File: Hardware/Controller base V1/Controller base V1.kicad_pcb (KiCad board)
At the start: 2 copper layers, 30 x 50 mm, 32 parts, among them J1 USB_C_Receptacle_USB2.0_16P, J3 Conn_02x10_Counter_Clockwise, J4 Conn_02x10_Counter_Clockwise, SW1 SW_Push, U1 AZ1117CH-3.3TRG1, U2 ESP32-S3-WROOM-1U-N4

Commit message: track update
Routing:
- net GND: track 72.2 -> 88.3 mm, vias 7 -> 11
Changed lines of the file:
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@@
+	)
+	(segment
+		(start 146.75 83.475)
+		(end 146.75 80.175)
+		(width 0.3)
+		(layer "F.Cu")
+		(net 1)
 	)
 	(segment
@@
 	)
 	(segment
+		(start 156.15 89.875)
+		(end 151.85 89.875)
+		(width 0.2)
+		(layer "F.Cu")
+		(net 1)
+	)
+	(segment
+		(start 151.85 89.875)
+		(end 146.75 84.775)
+		(width 0.2)
+		(layer "F.Cu")
+		(net 1)
+	)
+	(segment
 		(start 139.547624 75.985)
 		(end 138.93 75.985)
@@
 	(segment
 		(start 145.075 111)
-		(end 145.075 114.175)
+		(end 145.075 112.175)
 		(width 0.3)
 		(layer "F.Cu")
@@
 	)
 	(segment
+		(start 146.75 84.775)
+		(end 146.75 83.475)
+		(width 0.2)
+		(layer "F.Cu")
+		(net 1)
+	)
+	(segment
+		(start 145.075 112.175)
+		(end 145.075 114.175)
+		(width 0.3)
+		(layer "F.Cu")
+		(net 1)
+	)
+	(segment
 		(start 133.825 79.825)
 		(end 133.85 79.85)
@@
 	)
 	(via
+		(at 146.75 80.175)
+		(size 0.6)
+		(drill 0.3)
+		(layers "F.Cu" "B.Cu")
+		(net 1)
+	)
+	(via
+		(at 146.75 83.475)
+		(size 0.6)
+		(drill 0.3)
+		(layers "F.Cu" "B.Cu")
+		(free yes)
+		(net 1)
+	)
+	(via
 		(at 133.15 84.75)
 		(size 0.6)
@@
 	)
 	(via
+		(at 145.075 112.175)
+		(size 0.6)
+		(drill 0.3)
+		(layers "F.Cu" "B.Cu")
+		(net 1)
+	)
+	(via
 		(at 131.05 79.825)
 		(size 0.6)
 		(drill 0.3)
+		(layers "F.Cu" "B.Cu")
+		(net 1)
+	)
+	(via
+		(at 156.15 89.875)
+		(size 0.6)
+		(drill 0.3)

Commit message: update tracks
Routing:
- net GND: track 88.3 -> 85.0 mm, vias 11 -> 10
- net /CC2: track 6.91 -> 6.21 mm
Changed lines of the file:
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@@
-	)
-	(segment
-		(start 146.75 83.475)
-		(end 146.75 80.175)
-		(width 0.3)
-		(layer "F.Cu")
-		(net 1)
 	)
 	(segment
@@
 	)
 	(via
-		(at 146.75 80.175)
-		(size 0.6)
-		(drill 0.3)
-		(layers "F.Cu" "B.Cu")
-		(net 1)
-	)
-	(via
 		(at 146.75 83.475)
 		(size 0.6)
@@
 	)
 	(segment
-		(start 141.475 78.675)
-		(end 141.21 78.41)
+		(start 141.5125 78.325)
+		(end 141.21 78.0225)
 		(width 0.2)
 		(layer "F.Cu")
@@
 	)
 	(segment
-		(start 141.21 78.41)
+		(start 141.21 78.0225)
 		(end 141.21 76.92)
 		(width 0.2)
@@
 	)
 	(via
-		(at 141.475 78.675)
+		(at 141.5125 78.325)
 		(size 0.6)
 		(drill 0.3)
@@
 	)
 	(segment
-		(start 141.5125 78.6375)
-		(end 141.475 78.675)
-		(width 0.2)
-		(layer "B.Cu")
-		(net 12)
-	)
-	(segment
-		(start 141.5125 73.65)
-		(end 141.5125 78.6375)
-		(width 0.2)
-		(layer "B.Cu")
+		(start 141.5125 78.325)
+		(end 141.5125 73.65)
+		(width 0.2)
+		(layer "B.Cu")

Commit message: update
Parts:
- moved C7 1.82 mm to (149.1, 112.7)
- moved C5 1.78 mm to (149.1, 111.0)
- moved R6 1.52 mm to (148.6, 116.2)
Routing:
- net ESP_3.3V: track 13.7 -> 11.5 mm
- net GND: track 85.0 -> 86.3 mm, vias 10 -> 23

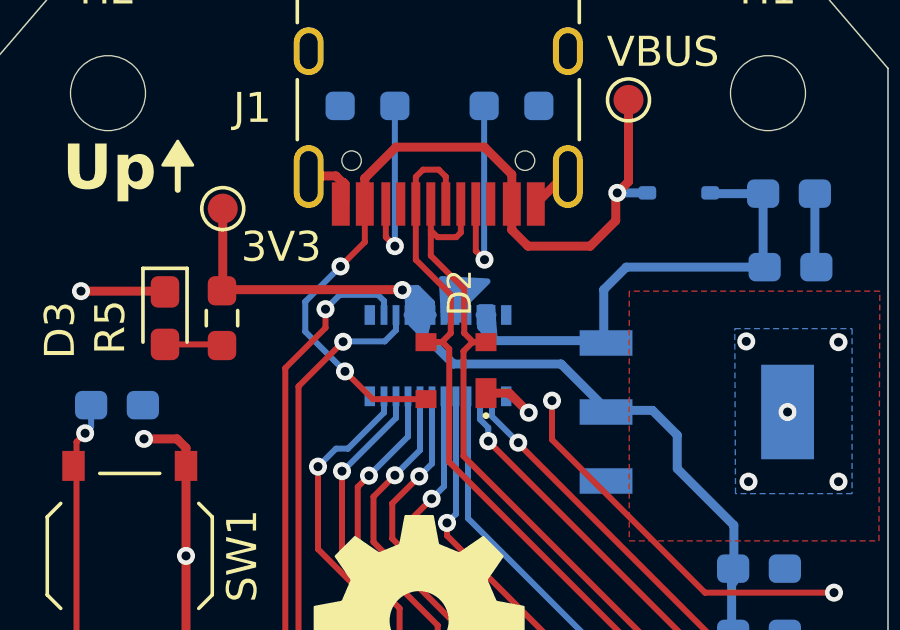
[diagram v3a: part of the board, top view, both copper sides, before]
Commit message: trace update
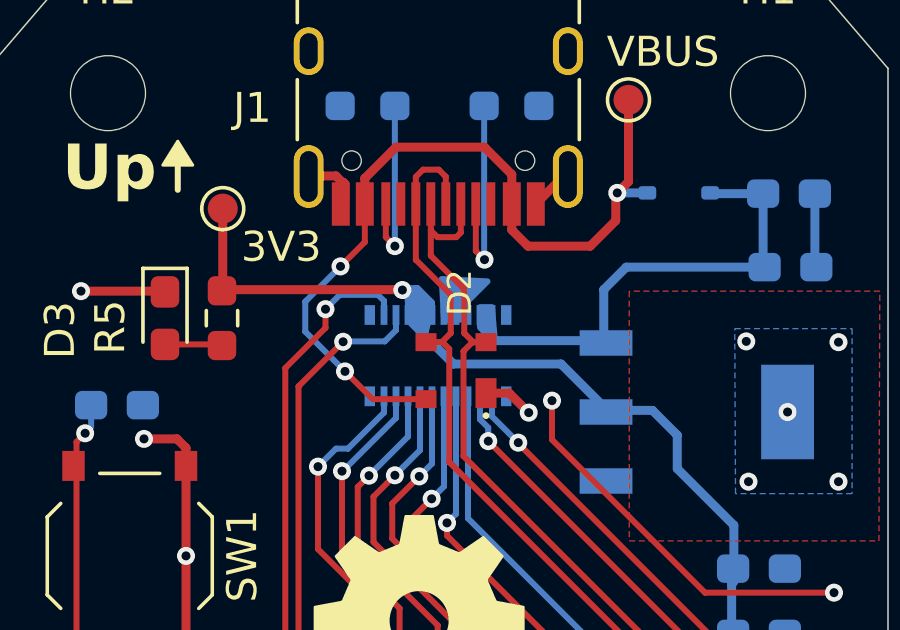
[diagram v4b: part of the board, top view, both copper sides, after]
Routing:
- net VCC_3V3: track 60.3 -> 59.4 mm
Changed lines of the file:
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@@
-	)
-	(segment
-		(start 142.75 80.62)
-		(end 142.595 80.62)
-		(width 0.3)
-		(layer "B.Cu")
-		(net 2)
 	)
 	(segment
@@
 		(start 150.9625 93.125)
 		(end 152.375 93.125)
-		(width 0.3)
-		(layer "B.Cu")
-		(net 2)
-	)
-	(segment
-		(start 141.95 80.62)
-		(end 142.75 80.62)
 		(width 0.3)
 		(layer "B.Cu")
@@
 	)
 	(segment
-		(start 144.575 80.62)
-		(end 144.75 80.62)
-		(width 0.3)
-		(layer "B.Cu")
-		(net 4)
-	)
-	(segment
 		(start 153.8375 79.025)
 		(end 149.225 79.025)
@@
 		(width 0.3)
 		(layer "B.Cu")
-		(net 4)
-	)
-	(segment
-		(start 144.35 80.62)
-		(end 144.575 80.62)
-		(width 0.3)
-		(layer "B.Cu")

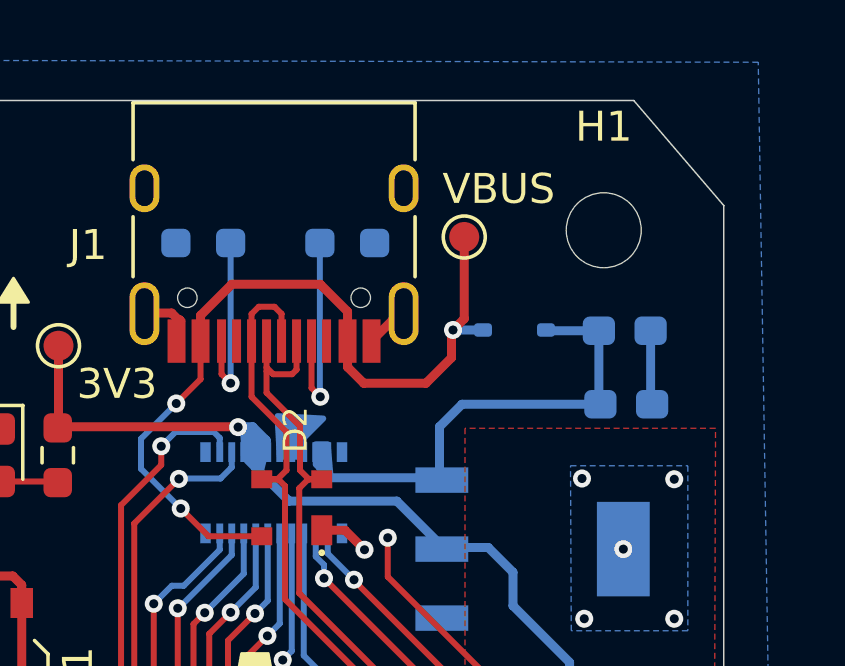
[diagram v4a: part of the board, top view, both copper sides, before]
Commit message: updated power trace for expansion
made where there is 5v to carrier board for future batter expansion
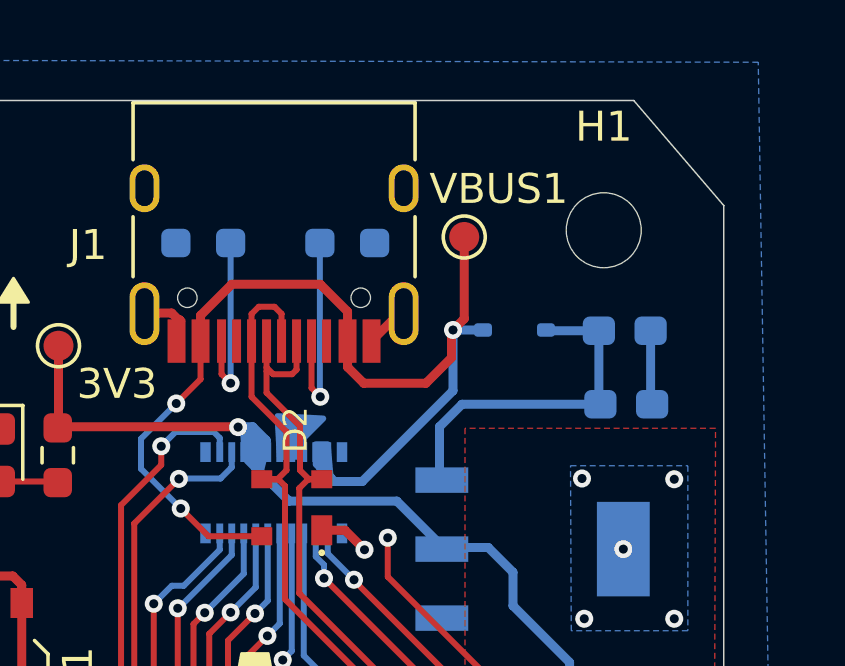
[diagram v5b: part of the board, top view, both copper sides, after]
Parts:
- renumbered VBUS to VBUS1
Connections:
- J3 pad 18: VCC_5V -> VBUS
- J3 pad 20: VCC_5V -> VBUS
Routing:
- net VBUS: track 27.7 -> 36.8 mm
- net VCC_5V: track 16.4 -> 11.7 mm
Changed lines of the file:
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@@
 		(descr "SMD pad as test Point, diameter 1.0mm")
 		(tags "test point SMD pad")
-		(property "Reference" "VBUS"
+		(property "Reference" "VBUS1"
 			(at 1.15 -1.6 0)
 			(layer "F.SilkS")
@@
 			(size 0.23 0.66)
 			(layers "B.Cu" "B.Mask" "B.Paste")
-			(net 4 "VCC_5V")
+			(net 5 "VBUS")
 			(pinfunction "18")
 			(pintype "passive")
@@
 			(size 0.23 0.66)
 			(layers "B.Cu" "B.Mask" "B.Paste")
-			(net 4 "VCC_5V")
+			(net 5 "VBUS")
 			(pinfunction "20")
 			(pintype "passive")
@@
 		(fill yes)
 		(layer "B.Cu")
-		(net 4)
+		(net 5)
 	)
 	(gr_poly
@@
 	)
 	(segment
-		(start 144.85 81.475)
-		(end 144.5125 81.1375)
-		(width 0.3)
-		(layer "B.Cu")
-		(net 4)
-	)
-	(segment
 		(start 153.7875 76.575)
 		(end 152.05 76.575)
@@
 	)
 	(segment
-		(start 144.5125 80.6825)
-		(end 144.575 80.62)
-		(width 0.3)
-		(layer "B.Cu")
-		(net 4)
-	)
-	(segment
 		(start 148.475 79.775)
 		(end 148.475 81.475)
@@
 	)
 	(segment
-		(start 148.475 81.475)
-		(end 144.85 81.475)
-		(width 0.3)
-		(layer "B.Cu")
-		(net 4)
-	)
-	(segment
 		(start 152.05 76.575)
 		(end 152.025 76.55)
@@
 	)
 	(segment
-		(start 144.5125 81.1375)
-		(end 144.5125 80.6825)
-		(width 0.3)
-		(layer "B.Cu")
-		(net 4)
-	)
-	(segment
 		(start 144.5 75.025)
 		(end 141.55 75.025)
@@
 	)
 	(segment
+		(start 144.85 81.475)
+		(end 144.5125 81.1375)
+		(width 0.3)
+		(layer "B.Cu")
+		(net 5)
+	)
+	(segment
+		(start 148.925 78.575)
+		(end 148.925 76.55)
+		(width 0.3)
+		(layer "B.Cu")
+		(net 5)
+	)
+	(segment
+		(start 144.5125 80.6825)
+		(end 144.575 80.62)
+		(width 0.3)
+		(layer "B.Cu")
+		(net 5)
+	)
+	(segment
+		(start 144.6 80.942307)
+		(end 144.6 81.225)
+		(width 0.3)
+		(layer "B.Cu")
+		(net 5)
+	)
+	(segment
 		(start 148.925 76.55)
 		(end 149.925 76.55)
@@
 	)
 	(segment
+		(start 145.9 81.6)
+		(end 148.925 78.575)
+		(width 0.3)
+		(layer "B.Cu")
+		(net 5)
+	)
+	(segment
 		(start 138.525 81.175)
 		(end 139.85 82.5)
@@
 		(layer "B.Cu")
 		(net 5)
+	)
+	(segment
+		(start 144.6 81.225)
+		(end 144.975 81.6)
+		(width 0.3)
+		(layer "B.Cu")
+		(net 5)
+	)
+	(segment
+		(start 144.975 81.6)
+		(end 145.9 81.6)
+		(width 0.3)
+		(layer "B.Cu")
+		(net 5)
+	)
+	(segment
+		(start 144.5125 81.1375)
+		(end 144.5125 80.6825)
+		(width 0.3)
+		(layer "B.Cu")
+		(net 5)
